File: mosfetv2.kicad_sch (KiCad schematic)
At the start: 25 parts, among them Q10 STL90N6F7, Q11 STL90N6F7, Q12 STL90N6F7, Q7 STL90N6F7, Q8 STL90N6F7, Q9 STL90N6F7

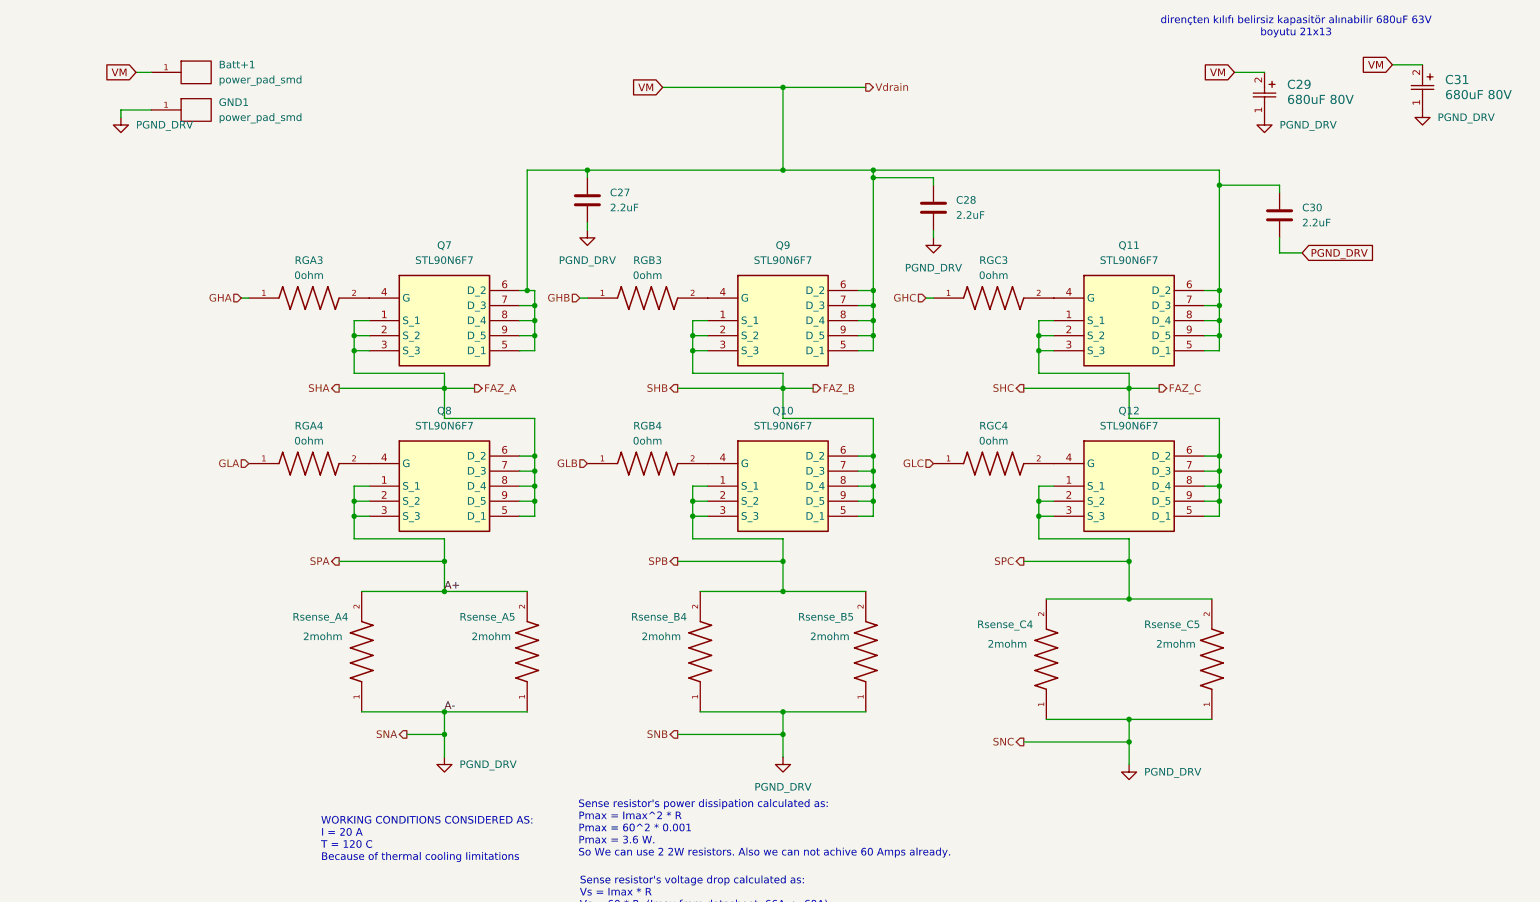
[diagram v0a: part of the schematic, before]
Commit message: New one_GND_Layer pcb desgin has finished yet. DRC Rule checks needs to be controlling and correcting still.
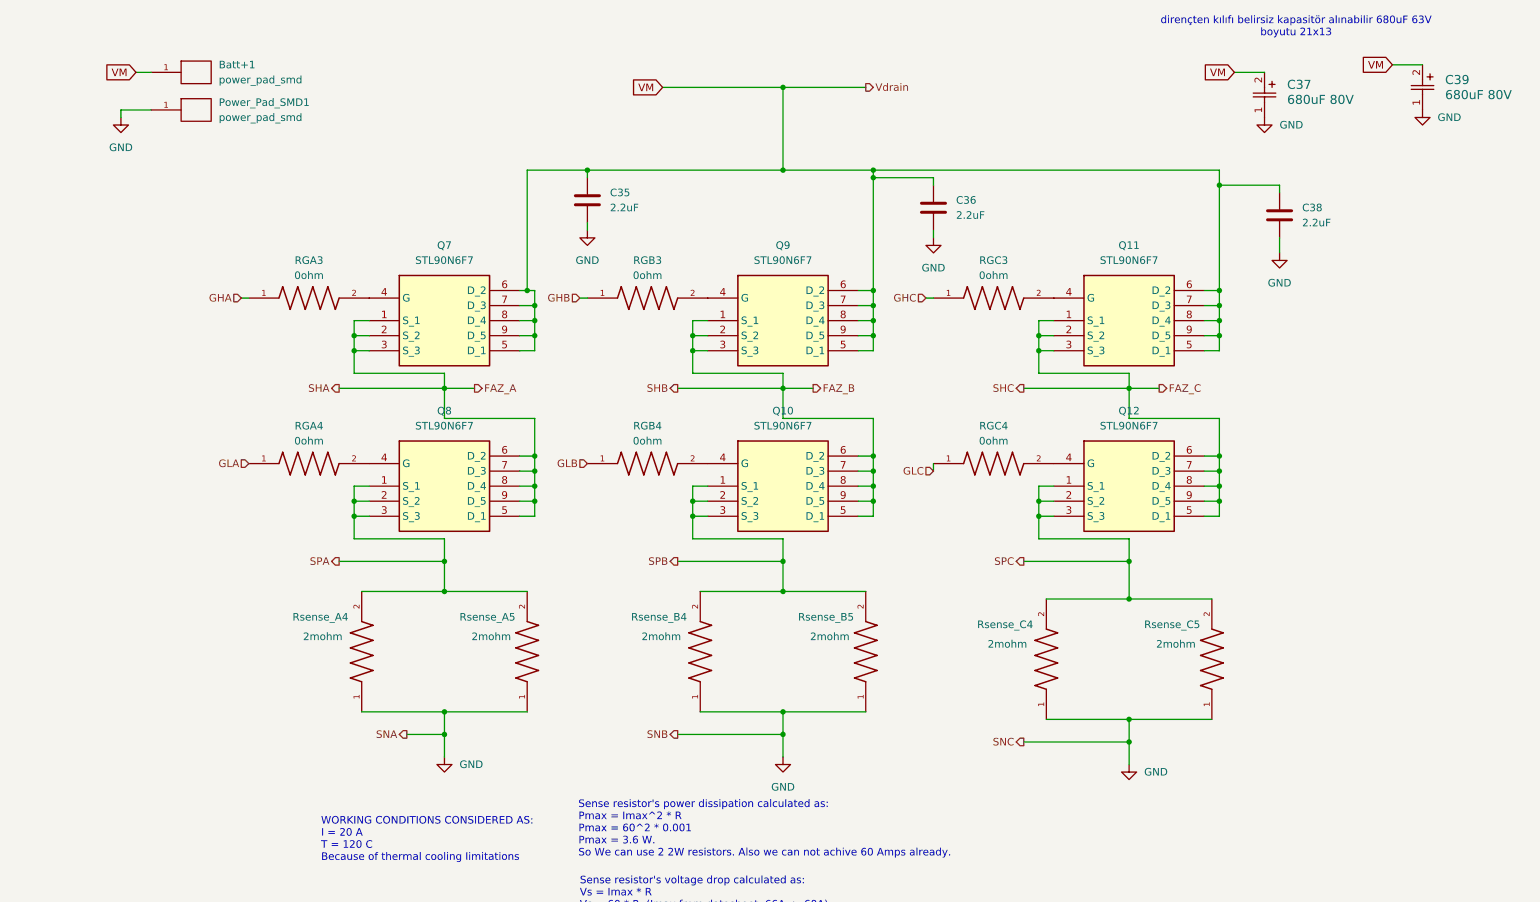
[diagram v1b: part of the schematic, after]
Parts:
- removed GND1: power_pad_smd, Pads:Power_pad_smd, symbol Power_Pad_smd:power_pad_smd
- added Power_Pad_SMD1: power_pad_smd, Pads:Power_pad_smd, symbol Power_Pad_smd:power_pad_smd
- renumbered C27 to C35, C28 to C36, C29 to C37, C30 to C38, C31 to C39
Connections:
- net PGND_DRV renamed GND
- net GND: now also Power_Pad_SMD1.1

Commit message: BOM list prepared for ekom and direnc.net
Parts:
- C35, C36, C38: footprint Capacitor_SMD:C_1206_3216Metric_Pad1.33x1.80mm_HandSolder -> Capacitor_SMD:C_0603_1608Metric_Pad1.08x0.95mm_HandSolder
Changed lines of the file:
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@@
 			)
 		)
-		(property "Footprint" "Capacitor_SMD:C_1206_3216Metric_Pad1.33x1.80mm_HandSolder"
+		(property "Footprint" "Capacitor_SMD:C_0603_1608Metric_Pad1.08x0.95mm_HandSolder"
 			(at 125.4252 52.07 0)
 			(effects
@@
 			)
 		)
-		(property "Footprint" "Capacitor_SMD:C_1206_3216Metric_Pad1.33x1.80mm_HandSolder"
+		(property "Footprint" "Capacitor_SMD:C_0603_1608Metric_Pad1.08x0.95mm_HandSolder"
 			(at 183.8452 53.34 0)
 			(effects
@@
 			)
 		)
-		(property "Footprint" "Capacitor_SMD:C_1206_3216Metric_Pad1.33x1.80mm_HandSolder"
+		(property "Footprint" "Capacitor_SMD:C_0603_1608Metric_Pad1.08x0.95mm_HandSolder"
 			(at 242.2652 54.61 0)
 			(effects

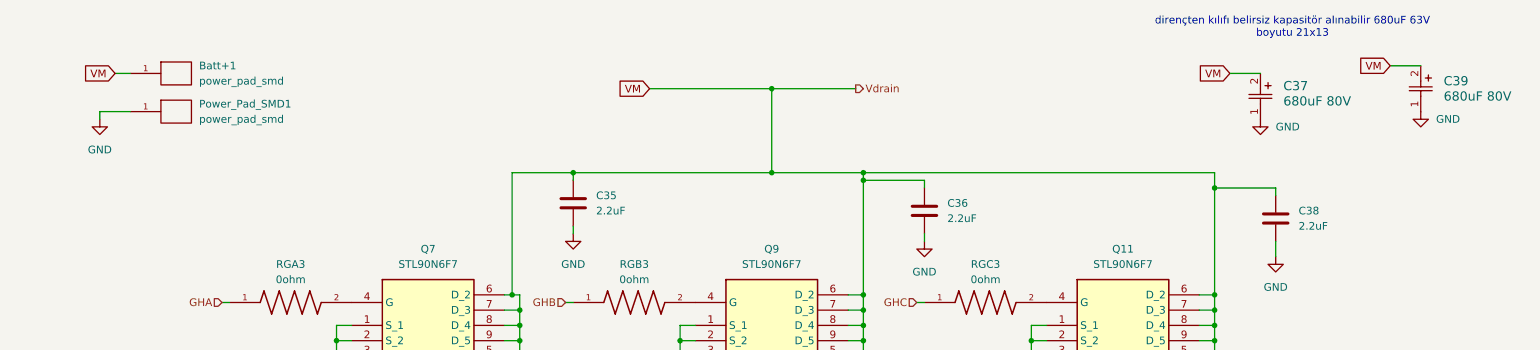
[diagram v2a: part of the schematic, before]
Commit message: for LCSC components the layout/footprints changed. Previous commit for ekom/direncnet components.
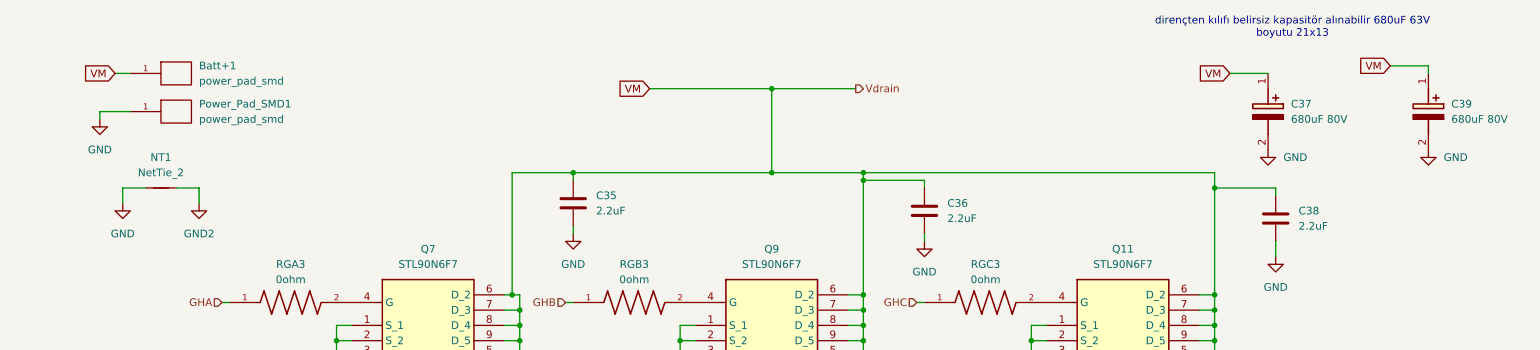
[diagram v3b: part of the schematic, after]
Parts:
- removed C37, C39: 680uF 80V, ul_80ZLJ680MGC18X25:80ZLJ680MGC18X25, symbol 2025-12-23_14-02-59:80ZLJ680MGC18X25
- added C37, C39: 680uF 80V, CAPPRD750W85D1600H2700, symbol EEUFS1K681:EEUFS1K681
- added NT1: NetTie_2, NetTie:NetTie-2_THT_Pad0.3mm, symbol Device:NetTie_2
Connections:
- net GND: now also C37.2 (-), C39.2 (-), NT1.1
- net VM: now also C37.1 (+), C39.1 (+)
- new net GND2: NT1.2
